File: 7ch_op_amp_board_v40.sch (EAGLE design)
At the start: 4 parts

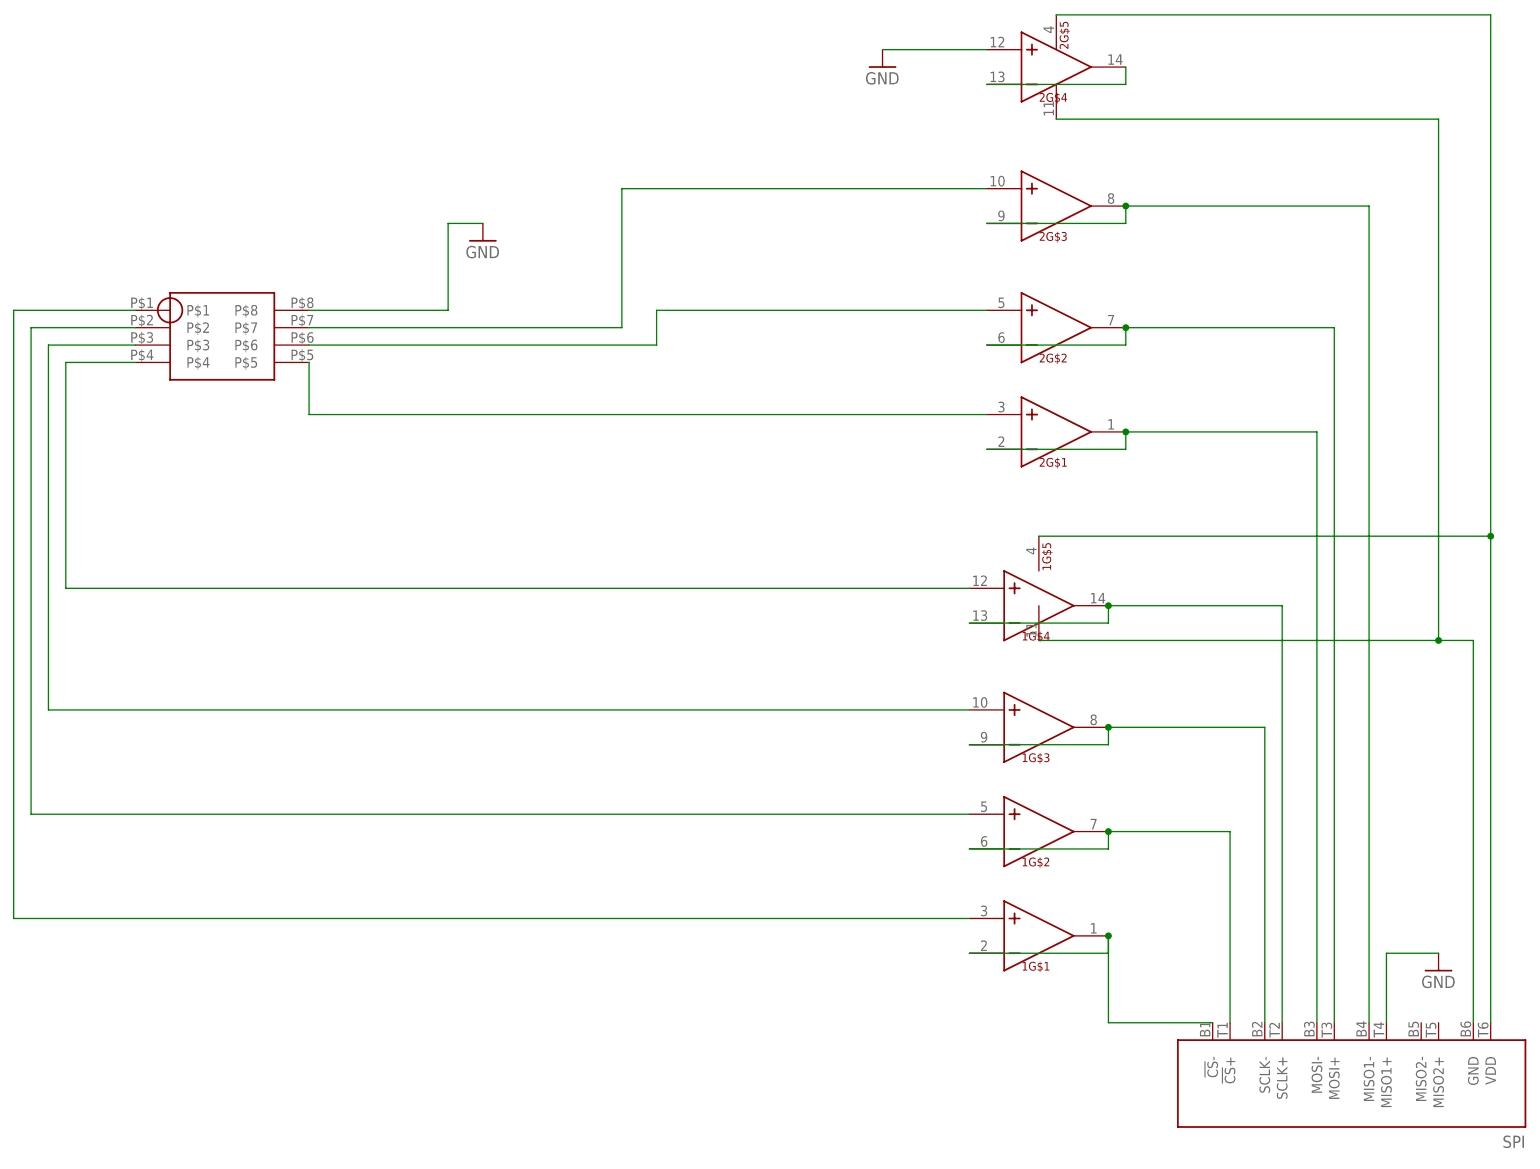
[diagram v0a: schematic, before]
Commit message: Replace connector with through-holes
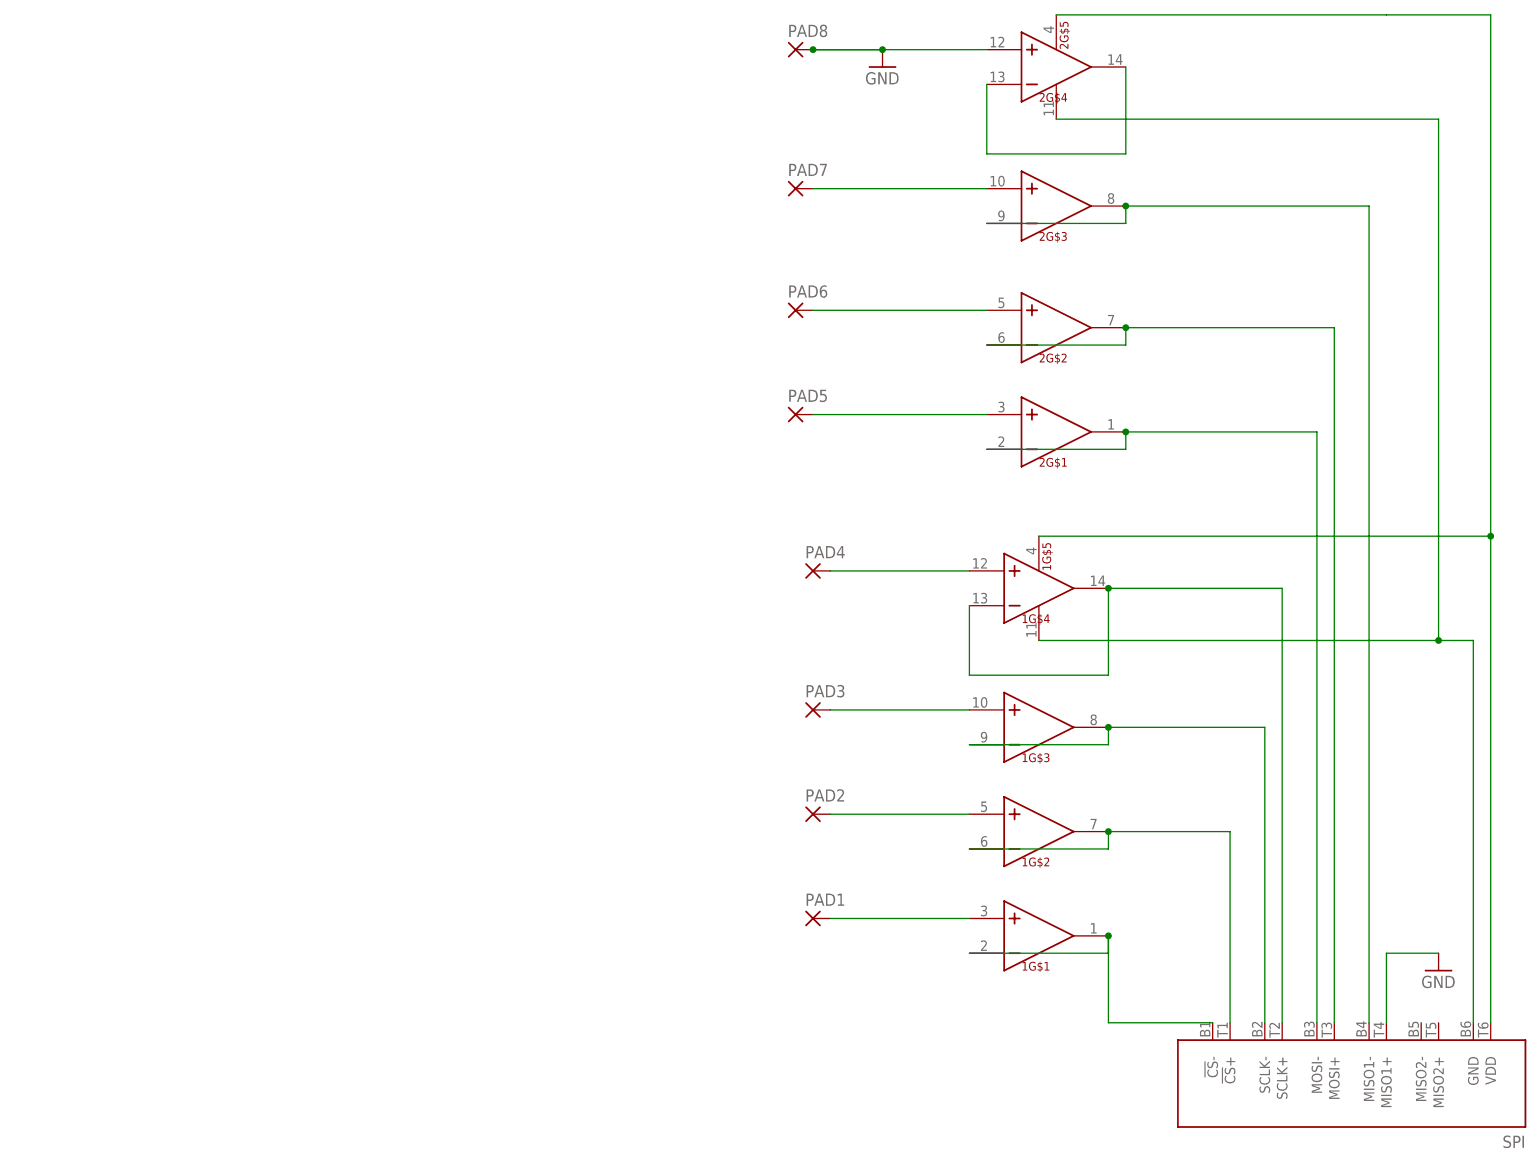
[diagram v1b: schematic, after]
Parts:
- removed B: 853-PPP-8-SOLDERTAIL, kjbrown:853-PPP-8-SOLDERTAIL
- added PAD1, PAD2, PAD3, PAD4, PAD5, PAD6, PAD7, PAD8: (no value), wirepad:1,6/0,8
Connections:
- removed net N$15: 2G$1.IN+, B.P$5
- removed net N$16: 2G$2.IN+, B.P$6
- removed net N$17: 2G$3.IN+, B.P$7
- new net N$21: 2G$3.IN+, PAD7.P
- new net N$22: 2G$2.IN+, PAD6.P
- new net N$23: 2G$1.IN+, PAD5.P
- net GND: now also PAD8.P; no longer B.P$8
- net N$11: now also 1G$2.IN+, PAD2.P; no longer 1G$1.IN+, B.P$1
- net N$12: now also 1G$3.IN+, PAD3.P; no longer 1G$2.IN+, B.P$2
- net N$13: now also 1G$4.IN+, PAD4.P; no longer 1G$3.IN+, B.P$3
- net N$8: now also 1G$1.IN+, PAD1.P; no longer 1G$4.IN+, B.P$4
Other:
- moved on the sheet: 1G$4
